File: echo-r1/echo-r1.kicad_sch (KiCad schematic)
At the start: 6 parts

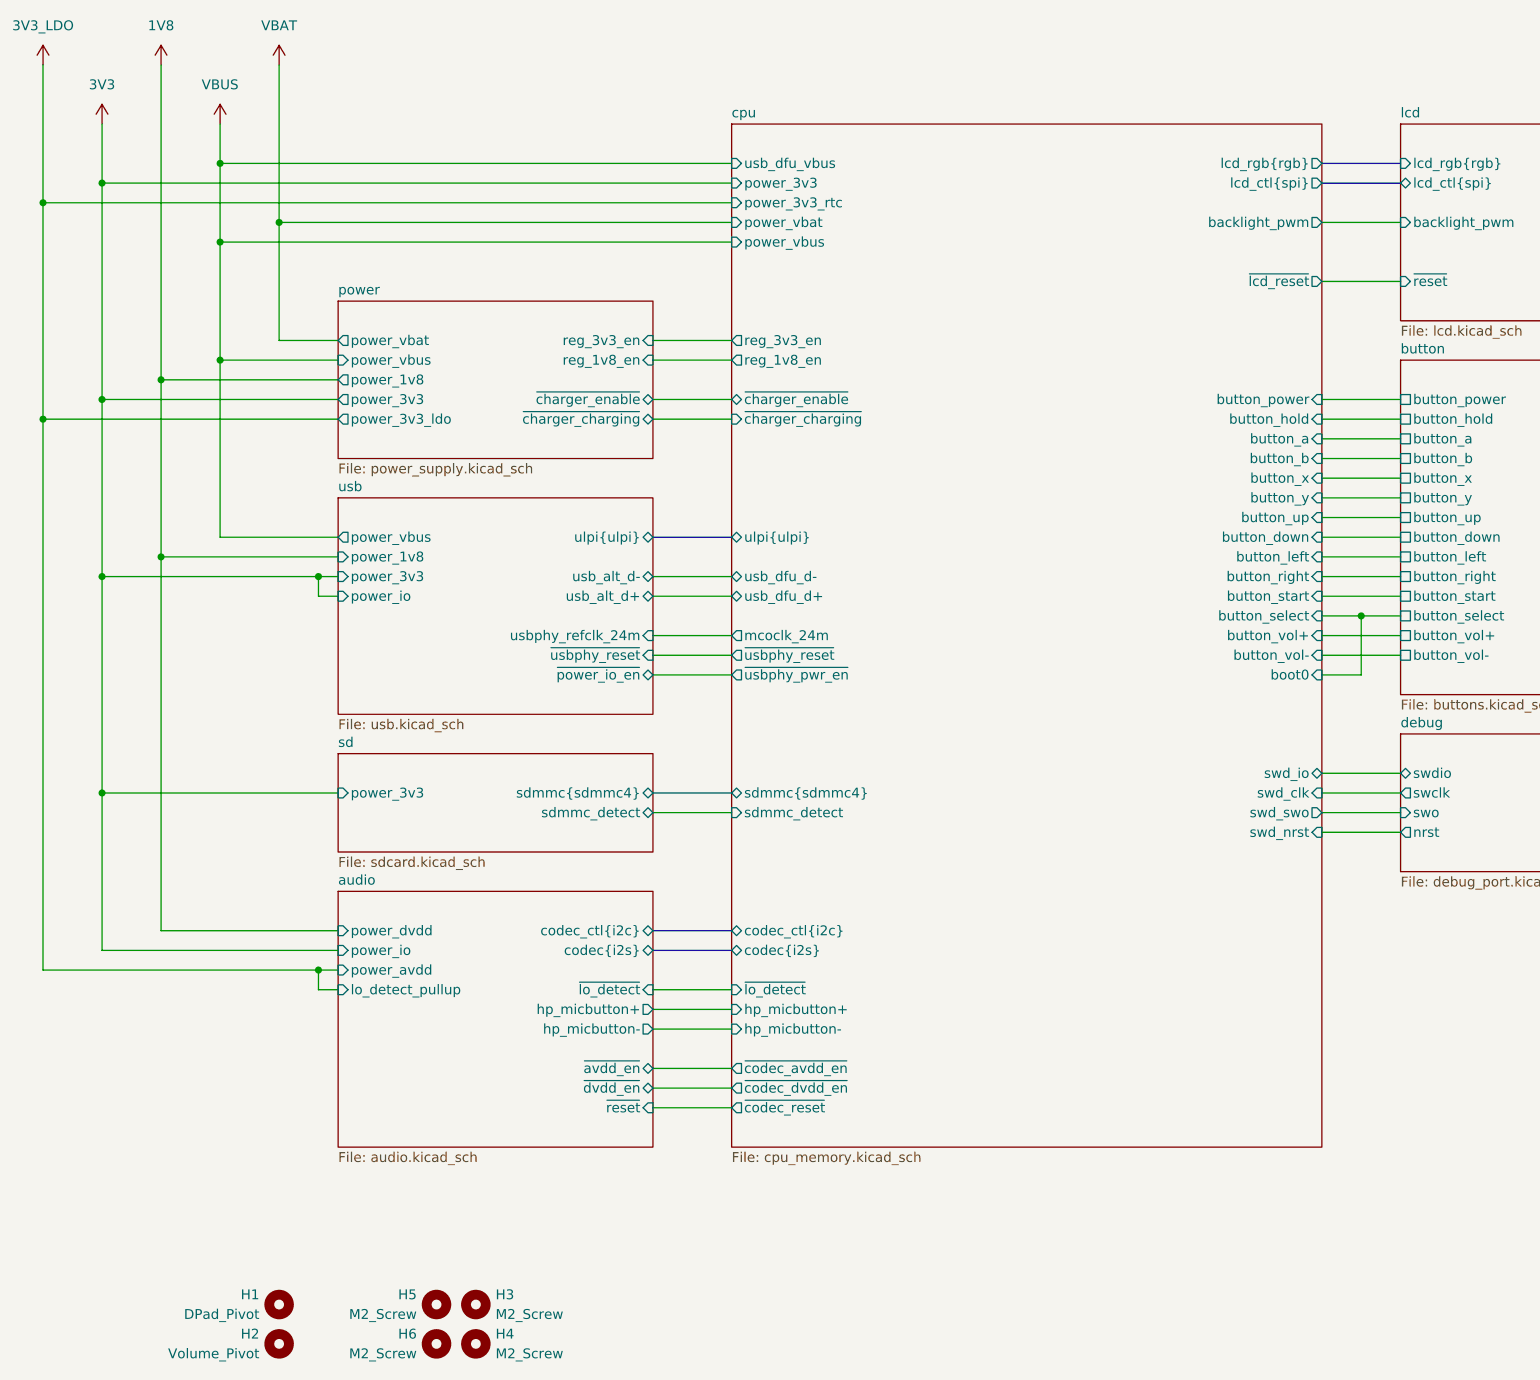
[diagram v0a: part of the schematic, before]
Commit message: WIP redesign with STM32H7R3Z8J6
The H7R3 has a bunch of features that greatly simplify the design:
support for HyperRAM, which requires far fewer pins than SDRAM and
is more power efficient; this frees up the FMC to interface with the
display in 8-bit 8080 MCU mode; and there is a built-in USB HS PHY,
removing the need for an external PHY.

The huge reduction in signal count allows for a smaller pin count
package -- only 144 pins. HyperRAM only comes in BGA packages so it
makes sense to also use the UFBGA-144 package for the CPU, which
takes up less than 1/4 of the board area of an LQFP-176 package.
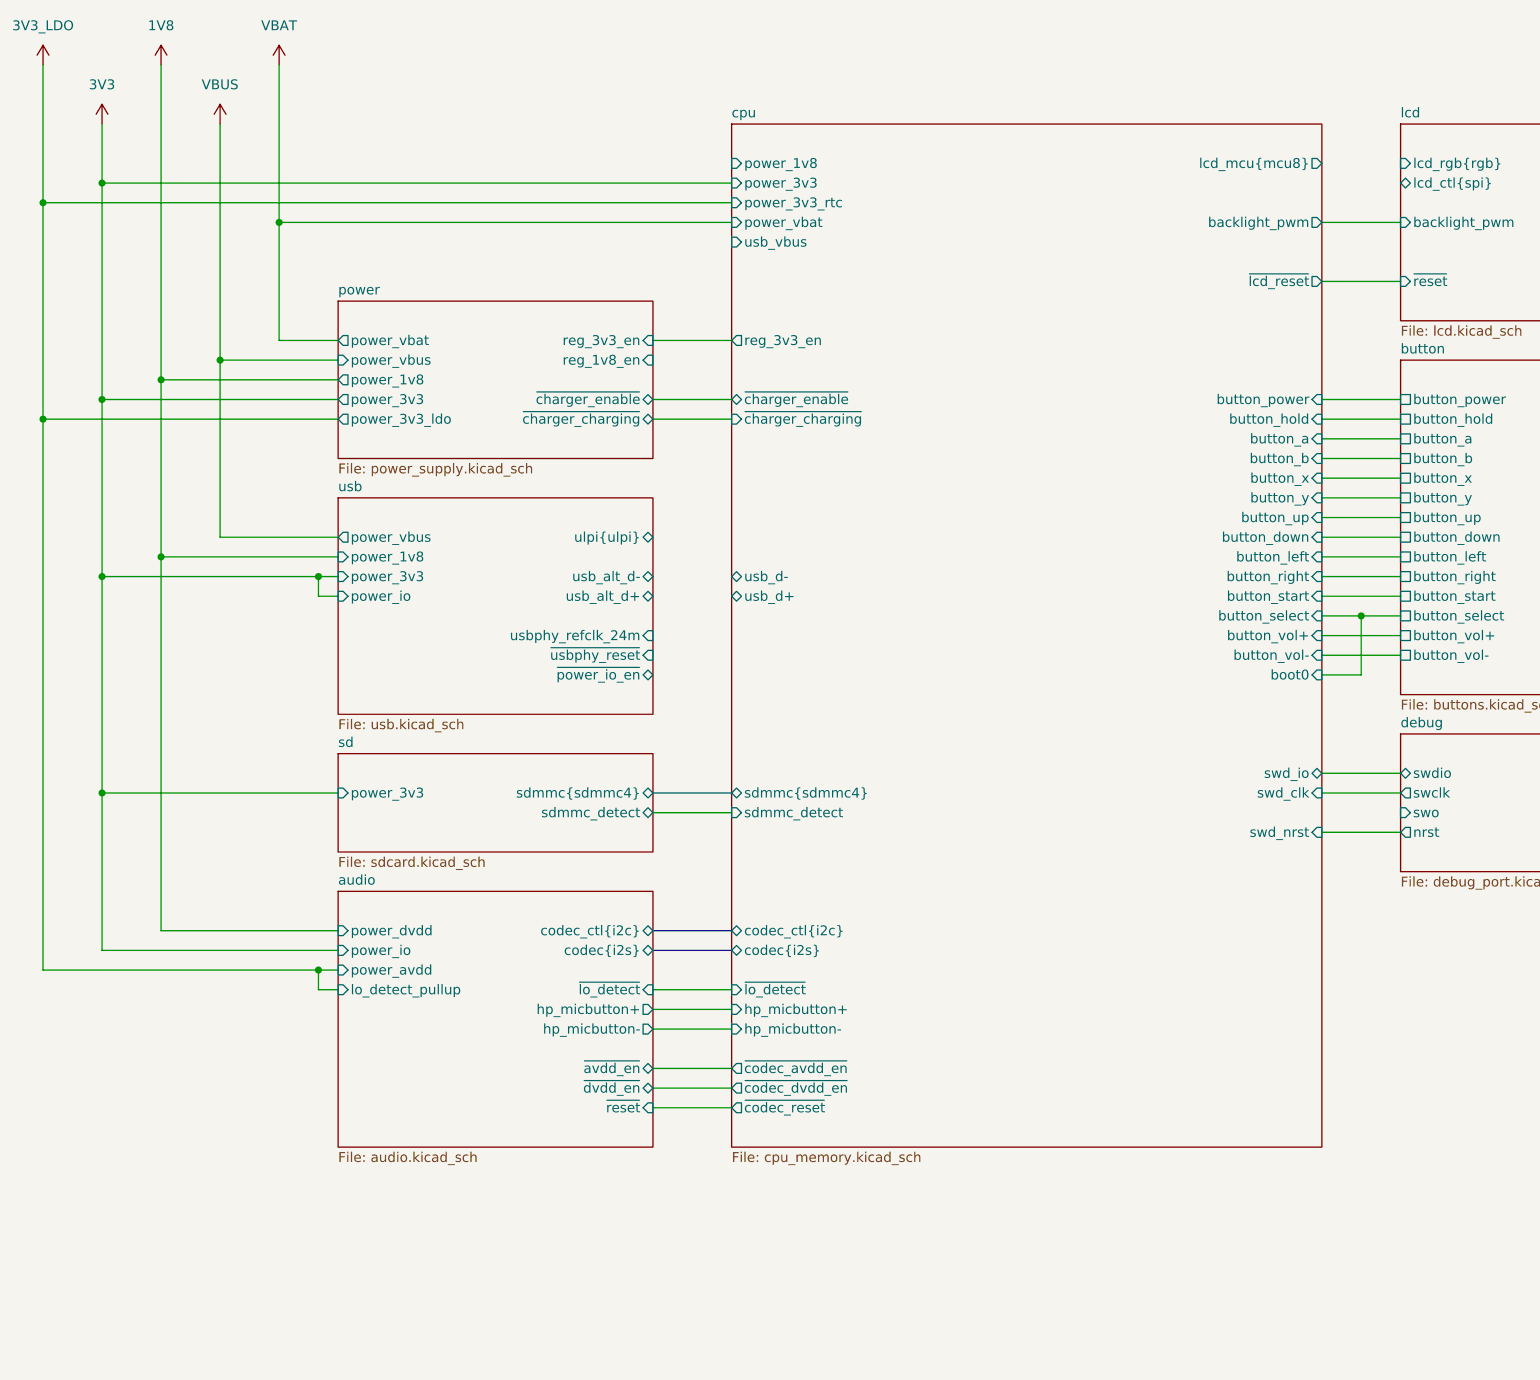
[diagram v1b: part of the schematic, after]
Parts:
- removed H1: DPad_Pivot, MountingHole:MountingHole_4mm, symbol Mechanical:MountingHole
- removed H2: Volume_Pivot, MountingHole:MountingHole_4mm, symbol Mechanical:MountingHole
- removed H3, H4, H5, H6: M2_Screw, MountingHole:MountingHole_2.2mm_M2, symbol Mechanical:MountingHole
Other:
- sheet cpu ports: added lcd_mcu{mcu8}, power_1v8, usb_d+, usb_d-, usb_vbus; removed lcd_ctl{spi}, lcd_rgb{rgb}, mcoclk_24m, power_vbus, reg_1v8_en, swd_swo, ulpi{ulpi}, usb_dfu_d+, usb_dfu_d-, usb_dfu_vbus, ~{usbphy_pwr_en}, ~{usbphy_reset}

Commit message: Continue with redesign, update and simplify schematic
- Consolidate small sheets (ports, etc) onto one page
- Add placeholders for STM32 external components
- Add power switch on SD card for resetting it
- Fix oversized input capacitors on voltage regulators
- Get rid of unique 1M resistor used in line-out detection
- Remove SOT23 TVS diodes (will be replaced by another package)
- Update LCD connector symbol for new 30pin screen
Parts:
- added C10, C12: 4 pF/NP0, Capacitor_SMD:C_0402_1005Metric, symbol Device:C_Small
- added C11, C9: 5 pF/NP0, Capacitor_SMD:C_0402_1005Metric, symbol Device:C_Small
- added C13: 22 µF, Capacitor_SMD:C_0603_1608Metric, symbol Device:C_Small
- added C25, C26, C27, C28, C29, C30, C31, C32, C33, C34, C36, C38, C50, C52, C54, C55: 100 nF, Capacitor_SMD:C_0402_1005Metric, symbol Device:C_Small
- added C35, C40, C44, C45, C49: 4.7 µF, Capacitor_SMD:C_0402_1005Metric, symbol Device:C_Small
- added C37, C39, C51, C53: 1 µF, Capacitor_SMD:C_0402_1005Metric, symbol Device:C_Small
- added C41, C43: 10 µF, Capacitor_SMD:C_0402_1005Metric, symbol Device:C_Small
- added C42: 220 pF, Capacitor_SMD:C_0402_1005Metric, symbol Device:C_Small
- added C46, C47, C48: 2.2 µF, Capacitor_SMD:C_0402_1005Metric, symbol Device:C_Small
- added D1, D2, D3, D4: 1N5819WS, Diode_SMD:D_SOD-323, symbol Device:D_Small
- added J2: TYPE-C-31-M-12, echoplayer:USB_C-Hroparts-TYPE-C-31-M-12, symbol Connector:USB_C_Receptacle_USB2.0_16P
- added J3: TF-115, echoplayer:microSD_XUNPU_TF-115, symbol Connector:Micro_SD_Card_Det1
- added J6: PM254-1-06-W-8.5, Connector_PinSocket_2.54mm:PinSocket_1x06_P2.54mm_Horizontal, symbol Connector_Generic:Conn_01x06
- added J7: ILI9342C, symbol Connector_Generic_MountingPin:Conn_01x30_MountingPin
- added L3: 2.2 µH, symbol Device:L_Small
- added Q4: AO3401A, Package_TO_SOT_SMD:SOT-23, symbol Device:Q_PMOS_GSD
- added R10, R12: 174 kΩ, Resistor_SMD:R_0603_1608Metric, symbol Device:R_Small_US
- added R11, R22, R25: 100 kΩ, Resistor_SMD:R_0402_1005Metric, symbol Device:R_Small_US
- added R13: 390 kΩ, Resistor_SMD:R_0603_1608Metric, symbol Device:R_Small_US
- added R14, R15: 5.1 kΩ, Resistor_SMD:R_0402_1005Metric, symbol Device:R_Small_US
- added R26, R27: 10 kΩ, Resistor_SMD:R_0402_1005Metric, symbol Device:R_Small_US
- added SW1: POWER, echoplayer:Switch_XKB_TS-1010-C-A, symbol echoplayer:SW_Push_MountingPin
- added SW10: DPAD→, echoplayer:Switch_ContactPad_10x3mm_Cross, symbol Switch:SW_Push
- added SW11: START, echoplayer:Switch_XUNPU_TS-1088-AR, symbol Switch:SW_Push
- added SW12: SELECT, echoplayer:Switch_XUNPU_TS-1088-AR, symbol Switch:SW_Push
- added SW13: VOL+, echoplayer:Switch_XKB_TS-1010-C-A, symbol echoplayer:SW_Push_MountingPin
- added SW14: VOL-, echoplayer:Switch_XKB_TS-1010-C-A, symbol echoplayer:SW_Push_MountingPin
- added SW2: HOLD, echoplayer:Switch_SHOUHAN_MSK12C02-HB, symbol echoplayer:SW_SPDT_MountingPin
- added SW3: A, echoplayer:Switch_ContactPad_10x3mm_Cross, symbol Switch:SW_Push
- added SW4: B, echoplayer:Switch_ContactPad_10x3mm_Cross, symbol Switch:SW_Push
- added SW5: X, echoplayer:Switch_ContactPad_10x3mm_Cross, symbol Switch:SW_Push
- added SW6: Y, echoplayer:Switch_ContactPad_10x3mm_Cross, symbol Switch:SW_Push
- added SW7: DPAD↑, echoplayer:Switch_ContactPad_10x3mm_Cross, symbol Switch:SW_Push
- added SW8: DPAD↓, echoplayer:Switch_ContactPad_10x3mm_Cross, symbol Switch:SW_Push
- added SW9: DPAD←, echoplayer:Switch_ContactPad_10x3mm_Cross, symbol Switch:SW_Push
- added U7: STM32H7R3Z8Jx, Package_BGA:UFBGA-144_10x10mm_Layout12x12_P0.8mm, symbol MCU_ST_STM32H7:STM32H7R3Z8Jx
- added U8: W958D8NBYA5I, echoplayer:TFBGA-24_6x8mm_Layout5x5_P1.0mm_Ball0.4mm, symbol echoplayer:W958D8NBYA5I
- added Y1: SC-32S32.768kHz20PPM12.5pF, Crystal:Crystal_SMD_3215-2Pin_3.2x1.5mm, symbol Device:Crystal
- added Y2: XTM32024000JT00351001, Crystal:Crystal_SMD_3225-4Pin_3.2x2.5mm, symbol Device:Crystal_GND24
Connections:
- net GND: now also C10.2, C11.2, C12.2, C13.2, C25.2, C26.2, C27.2, C9.2, J2.A1 (GND), J2.A12 (GND), J2.B1 (GND), J2.B12 (GND), J2.S1 (SHIELD), J3.10 (SHIELD), J3.6 (VSS), J6.4 (Pin_4), J7.1 (Pin_1), R11.2, R13.2, R14.1, R15.1, R22.2, U7.A1 (VSS), U7.A12 (VSS), U7.C9 (VSS), U7.D2 (VSS), U7.D5 (VSS), U7.D7 (VSS), U7.D8 (VSSUSB), U7.E1 (VSSSMPS), U7.E7 (VSS), U7.F5 (VSS), U7.G1 (VSS), U7.G8 (VSS), U7.H3 (VSSA), U7.H4 (VSS), U7.H7 (VSS), U7.K10 (VSS), U7.K6 (VSS), U7.K8 (VSS), U7.M1 (VSS), U7.M12 (VSS), U8.B3 (VSS), U8.C1 (VSSQ), U8.E5 (VSSQ), Y2.2, Y2.4
- net VBUS: now also D4.2 (A), J2.A4 (VBUS), J2.A9 (VBUS), J2.B4 (VBUS), J2.B9 (VBUS), R10.2, U7.B8 (PM8)
- net power/reg_1v8_en: now also D1.1 (K), D2.1 (K), D3.1 (K), D4.1 (K)
- new net: J2.A5 (CC1), R14.2
- new net: J2.B5 (CC2), R15.2
- new net: U8.A5 (RFU), U8.B5 (RFU), U8.C2 (RFU), U8.C5 (RFU)
- new net +1V8: C25.1, C26.1, C27.1, U7.K5 (VDDXSPI1), U7.K7 (VDDXSPI1), U7.K9 (VDDXSPI1), U8.B4 (VCC), U8.D1 (VCCQ), U8.E4 (VCCQ)
- new net +3V3: C13.1, J6.6 (Pin_6), J7.4 (Pin_4), J7.5 (Pin_5), Q4.2 (S), R25.1, R26.1, R27.1, U7.A10 (VDD33USB), U7.A11 (VDD50USB), U7.D6 (VDD), U7.D9 (VDD), U7.E4 (VDD), U7.E5 (VCAP4), U7.F2 (VDDSMPS), U7.F6 (VDDLDO), U7.F7 (VDDLDO), U7.F8 (VCAP3), U7.F9 (VDD), U7.G4 (VDD), U7.G6 (VDDLDO), U7.G7 (VDDLDO), U7.H6 (VCAP1), U7.H8 (VCAP2), U7.J3 (VDDA), U7.J5 (VDD), U7.J9 (VDD)
- new net +3V3_LDO: U7.B1 (VBAT)
- new net adc_vbat: R12.2, R13.1
- new net adc_vbus: R10.1, R11.1
- new net button_a: SW3.2
- new net button_b: SW4.2
- new net button_down: SW8.2
- new net button_hold: SW2.3 (C)
- new net button_left: SW9.2
- new net button_power: D3.2 (A), SW1.2
- new net button_right: SW10.2
- new net button_select: SW12.2
- new net button_start: SW11.2
- new net button_up: SW7.2
- new net button_vol+: SW13.2
- new net button_vol-: SW14.2
- new net button_x: SW5.2
- new net button_y: SW6.2
- new net codec.bclk: U7.D1 (PE5)
- new net codec.dplay: U7.E2 (PE6)
- new net codec.drec: U7.D3 (PE3)
- new net codec.mclk: U7.C4 (PE2)
- new net codec.wclk: U7.E3 (PE4)
- new net codec_ctl.scl: R26.2, U7.A2 (PB8)
- new net codec_ctl.sda: R27.2, U7.D4 (PB7)
- new net cpu_power_on: D1.2 (A)
- new net lcd.cs: J7.11 (Pin_11)
- new net lcd.d0: J7.13 (Pin_13), U7.E11 (PA12)
- new net lcd.d1: J7.14 (Pin_14), U7.F12 (PA11)
- new net lcd.d2: J7.15 (Pin_15), U7.F11 (PA10)
- new net lcd.d3: J7.16 (Pin_16), U7.G12 (PA9)
- new net lcd.d4: J7.17 (Pin_17), U7.F10 (PA8)
- new net lcd.d5: J7.18 (Pin_18), U7.L1 (PA2)
- new net lcd.d6: J7.19 (Pin_19), U7.J2 (PA1)
- new net lcd.d7: J7.20 (Pin_20), U7.K1 (PA0)
- new net lcd.dcx: J7.6 (Pin_6), U7.G5 (PC1)
- new net lcd.wrx: J7.10 (Pin_10), U7.L5 (PB2)
- new net lcd_im0_im3: J7.30 (Pin_30)
- new net lcd_im1: J7.29 (Pin_29)
- new net lcd_led_a: J7.3 (Pin_3)
- new net lcd_led_k: J7.2 (Pin_2)
- new net lcd_mcu.cs: U7.K11 (PD12)
- new net lcd_reset: J7.9 (Pin_9), R22.1
- new net nrst: J6.2 (Pin_2)
- new net osc24m_in: C10.1, U7.G2 (PH0), Y2.1
- new net osc24m_out: C12.1, U7.H1 (PH1), Y2.3
- new net osc32k_in: C9.1, U7.C1 (PC14), Y1.1
- new net osc32k_out: C11.1, U7.C2 (PC15), Y1.2
- new net power_vbat: R12.1
- new net rtc_wakeup: D2.2 (A), U7.B2 (PC13)
- new net sdmmc.clk: J3.5 (CLK), U7.C12 (PC12)
- new net sdmmc.cmd: J3.3 (CMD), U7.C11 (PD2)
- new net sdmmc.d0: J3.7 (DAT0), U7.G11 (PC8)
- new net sdmmc.d1: J3.8 (DAT1), U7.G10 (PC9)
- new net sdmmc.d2: J3.1 (DAT2), U7.D11 (PC10)
- new net sdmmc.d3: J3.2 (DAT3/CD), U7.E9 (PC11)
- new net sdmmc_detect: J3.9 (DET)
- new net sdmmc_pwr: J3.4 (VDD), Q4.3 (D)
- new net swclk: J6.5 (Pin_5)
- new net swd_clk: U7.E10 (PA14(JTCK)
- new net swd_io: U7.E12 (PA13(JTMS)
- new net swd_nrst: U7.F4 (NRST)
- new net swdio: J6.3 (Pin_3)
- new net usb_d+: J2.A6 (D+), J2.B6 (D+), U7.A9 (PM6)
- new net usb_d-: J2.A7 (D-), J2.B7 (D-), U7.B9 (PM5)
- new net xspi.ck+: U7.M7 (PO4), U8.B2 (CK)
- new net xspi.ck-: U7.L7 (PO5), U8.A2 (CK#)
- new net xspi.cs: U7.J7 (PO0), U8.A3 (CS#)
- new net xspi.d0: U7.L8 (PP0), U8.D3 (DQ0)
- new net xspi.d1: U7.L10 (PP1), U8.D2 (DQ1)
- new net xspi.d2: U7.L6 (PP2), U8.C4 (DQ2)
- new net xspi.d3: U7.M6 (PP3), U8.D4 (DQ3)
- new net xspi.d4: U7.M5 (PP4), U8.D5 (DQ4)
- new net xspi.d5: U7.M8 (PP5), U8.E3 (DQ5)
- new net xspi.d6: U7.M9 (PP6), U8.E2 (DQ6)
- new net xspi.d7: U7.M10 (PP7), U8.E1 (DQ7)
- new net xspi.dqs0: U7.L9 (PO2), U8.C3 (RWDS)
- new net xspi_reset: U8.A4 (RESET#)
- new net ~{sdmmc_pwr_en}: Q4.1 (G), R25.2
- no-connect marks 0 -> 20
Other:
- removed sheet button
- removed sheet cpu
- removed sheet debug
- removed sheet lcd
- removed sheet sd
- removed sheet usb
- note added: "24M CRYSTAL"
- note added: "32K CRYSTAL"
- note added: "ADC INPUT SCALING"
- note added: "AUDIO OUTPUT/INPUT"
- note added: "BUTTONS"
- note added: "CPU"
- note added: "Contact pad buttons designed to 10x3xH5mm spec, eg: https://www.aliexpress.com/item/1005003589789322.html"
- note added: "DB8-DB15 unused"
- note added: "Decoupling capacitor"
- note added: "HYPERRAM MEMORY"
- note added: "LCD CONNECTOR"
- note added: "MEMORY CARD"
- note added: "NOTE: VBUS is discharged by the ADC voltage divider when unplugged"
- note added: "POWER SUPPLY"
- note added: "Power switch for resetting the card"
- note added: "SWD DEBUG PORT"
- note added: "TODO add new TVS diodes"
- note added: "USB-C CONNECTOR"
- note added: "VBAT decoupling"
- note added: "VCAP decoupling (Probably not needed)"
- note added: "VDD decoupling"
- note added: "VDD33USB"
- note added: "VDD50USB"
- note added: "VDDA decoupling"
- note added: "VDDSMPS decoupling best performance"
- note added: "VDDXSPI1"
- note added: "VLXSMPS parts"
- note added: "maithoga 2.31 inch 30PIN SPI TFT LCD Horizontal Screen COG ILI9342C Driver IC 320(RGB)*240 MCU 8/16Bit Interface"
- note removed: "POWER must be active high to power on the machine. SELECT is active high so it can set the BOOT0 pin level."
